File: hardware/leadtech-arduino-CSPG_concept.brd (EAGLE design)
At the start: 53.3 x 80 mm, 49 parts, among them IC1 OP-AMP, IC3 4050D, J1 CON_HEADER_1X08-PTH, J2 CON_HEADER_1X04, J3 CON_HEADER_1X03-PTH, J9 CON_HEADER_1X02-PTH, Q1 16Mhz, U1 DS1302, U3 PL2303HX

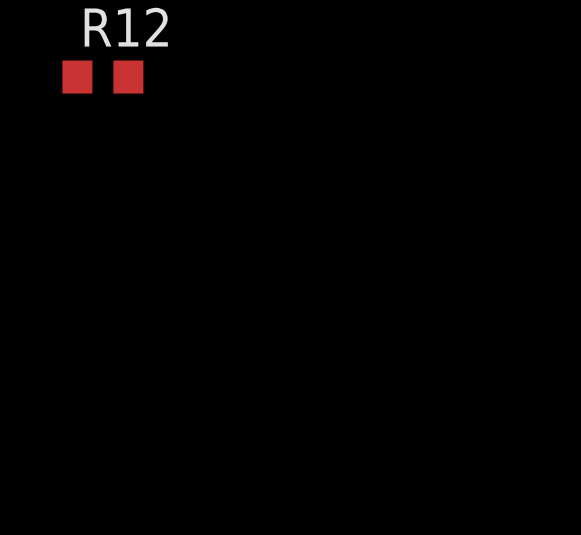
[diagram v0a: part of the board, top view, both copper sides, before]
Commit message: add power source manager op-amp wiring
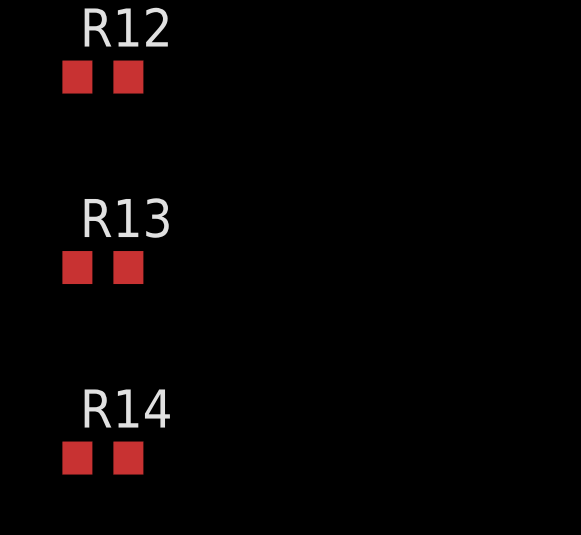
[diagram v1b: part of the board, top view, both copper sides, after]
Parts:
- added R13, R14: 10K, dp_devices.v6:R603
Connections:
- new net N$6: IC1.6, IC1.7
- new net N$9: IC1.5, R13.1, R14.2
- net +5V: now also R13.2
- net GND: now also R14.1
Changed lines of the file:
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@@
 <attribute name="VALUE" x="-24.892" y="-25.146" size="1.27" layer="27" font="vector" ratio="10"/>
+</element>
+<element name="R13" library="dp_devices.v6" package="R603" value="10K" x="-24.13" y="-29.21" smashed="yes">
+<attribute name="NAME" x="-24.892" y="-28.194" size="1.27" layer="25" font="vector" ratio="10"/>
+<attribute name="VALUE" x="-24.892" y="-31.496" size="1.27" layer="27" font="vector" ratio="10"/>
+</element>
+<element name="R14" library="dp_devices.v6" package="R603" value="10K" x="-24.13" y="-35.56" smashed="yes">
+<attribute name="NAME" x="-24.892" y="-34.544" size="1.27" layer="25" font="vector" ratio="10"/>
+<attribute name="VALUE" x="-24.892" y="-37.846" size="1.27" layer="27" font="vector" ratio="10"/>
 </element>
 </elements>
@@
 <contactref element="C1" pad="-"/>
 <contactref element="R12" pad="1"/>
+<contactref element="R14" pad="1"/>
 <wire x1="77.47" y1="76.2" x2="84.3534" y2="71.755" width="0" layer="19" extent="1-1"/>
 <wire x1="80.43" y1="59.69" x2="84.3534" y2="71.755" width="0" layer="19" extent="1-1"/>
@@
 <wire x1="-24.46" y1="-13.97" x2="-15" y2="-15.85" width="0" layer="19" extent="1-1"/>
 <wire x1="-24.98" y1="-22.86" x2="-24.46" y2="-13.97" width="0" layer="19" extent="1-1"/>
+<wire x1="-24.98" y1="-35.56" x2="-24.98" y2="-22.86" width="0" layer="19" extent="1-1"/>
 <wire x1="82.13" y1="22.86" x2="80.43" y2="59.69" width="0" layer="19" extent="1-1"/>
 <wire x1="86.995" y1="14.17" x2="82.13" y2="22.86" width="0" layer="19" extent="1-1"/>
@@
 <contactref element="VREG2" pad="3"/>
 <contactref element="Q2" pad="2"/>
+<contactref element="R13" pad="2"/>
 <wire x1="80.43" y1="22.86" x2="96.1" y2="41.91" width="0" layer="19" extent="1-1"/>
 <wire x1="83.185" y1="14.17" x2="80.43" y2="22.86" width="0" layer="19" extent="1-1"/>
@@
 <wire x1="-5.4" y1="-9.99" x2="1.905" y2="-7.36" width="0" layer="19" extent="1-1"/>
 <wire x1="-10.4" y1="-15.85" x2="-5.4" y2="-9.99" width="0" layer="19" extent="1-1"/>
+<wire x1="-23.28" y1="-29.21" x2="-10.4" y2="-15.85" width="0" layer="19" extent="1-1"/>
 </signal>
 <signal name="N$8">
@@
 <wire x1="-5.5" y1="-16.51" x2="5.08" y2="40.64" width="0" layer="19" extent="1-1"/>
 </signal>
+<signal name="N$6">
+<contactref element="IC1" pad="6"/>
+<contactref element="IC1" pad="7"/>
+<wire x1="3.175" y1="-7.36" x2="4.445" y2="-7.36" width="0" layer="19" extent="1-1"/>
+</signal>
+<signal name="N$9">
+<contactref element="IC1" pad="5"/>
+<contactref element="R13" pad="1"/>
+<contactref element="R14" pad="2"/>
+<wire x1="-24.98" y1="-29.21" x2="-23.28" y2="-35.56" width="0" layer="19" extent="1-1"/>
+<wire x1="5.715" y1="-7.36" x2="-24.98" y2="-29.21" width="0" layer="19" extent="1-1"/>
+</signal>
 </signals>

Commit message: continue routing board
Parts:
- removed VREG1: 7805, dp_devices.v6:TO-220V
- removed VREG2: 3.3V, dp_devices.v6:SOT-223
- added C16: 0.1uF, rcl:C0603
- added J4: CON_HEADER_1X02-PTH, dp_devices.v6:M1X2
- added U2: VREG-78M05, trosh_devices.eagle.v9:DPAK-3
- added U4: MP1584EN_MODULE, trosh_devices.eagle.v9:MP1584EN_DCDC_MODULE
- added U5: VREG-RT9163-3.3V, trosh_devices.eagle.v9:SOT-223
- moved C5 86.2 mm to (68.3, 6.35), turned to 270 degrees
- moved USB1 85.4 mm to (74.7, 14.0), turned to 90 degrees
- moved R12 80.7 mm to (44.5, 19.7), turned to 90 degrees
- moved L1 79.3 mm to (68.3, 10.8), turned to 90 degrees
- moved C1 78.4 mm to (39.4, 33.7), turned to 270 degrees
- moved C4 77.1 mm to (57.1, 5.08)
- moved R3 73.6 mm to (65.4, 12.1), turned to 180 degrees
- moved L2 71.8 mm to (68.3, 17.1), turned to 270 degrees
- moved R4 71.4 mm to (65.4, 14.0), turned to 180 degrees
- moved Q2 70.4 mm to (57.1, 21.6), turned to 180 degrees
- moved R14 70.4 mm to (7.62, 27.3), turned to 270 degrees
- moved R6 69.2 mm to (65.4, 15.9), turned to 180 degrees
- moved R5 68.7 mm to (26.7, 45.7), turned to 90 degrees
- moved R13 65.8 mm to (9.53, 27.3), turned to 270 degrees
- moved U3 65.2 mm to (57.1, 11.4), turned to 270 degrees
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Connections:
- new net N$7: J4.1, U4.3, U4.4
- net +3V3: now also U5.3; no longer VREG2.2
- net +5V: now also C16.2, U2.3, U5.1; no longer VREG1.2, VREG2.3
- net GND: now also C16.1, J4.2, U2.2, U4.1, U4.2, U4.7, U4.8, U5.2, U5.4; no longer VREG1.1, VREG2.1
- net N$19: now also U4.5, U4.6
- net VIN: now also U2.1; no longer VREG1.3
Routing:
- net +5V: track 0.00 -> 41.8 mm, vias 0 -> 2
- net VUSB: track 0.00 -> 33.6 mm, vias 0 -> 3
- net VO33: track 0.00 -> 30.6 mm
- net N$4: track 0.00 -> 13.6 mm, vias 0 -> 2
- net N$19: track 0.00 -> 12.5 mm
- net N$14: track 0.00 -> 11.9 mm
- net VIN: track 0.00 -> 9.40 mm
- net N$7: track 0.00 -> 9.08 mm
- net N$13: track 0.00 -> 8.23 mm
- net N$12: track 0.00 -> 7.23 mm
- net N$11: track 0.00 -> 5.78 mm
- net N$21: track 0.00 -> 3.26 mm
- net N$17: track 0.00 -> 2.65 mm
- net N$18: track 0.00 -> 2.37 mm
- added copper zone on layer 1, net GND
- added copper zone on layer 1, net N$15
- added copper zone on layer 1, net N$16
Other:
- board size 53.3 x 80 mm -> 80 x 53.3 mm

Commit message: routing
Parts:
- added J5: CON_HEADER_1X02-PTH, dp_devices.v6:M1X2
- moved C14 34.4 mm to (85.1, 40.6)
- moved C3 23.8 mm to (26.7, 50.8), turned to 270 degrees
- moved C2 23.5 mm to (21.6, 50.8), turned to 90 degrees
- moved J9 22.0 mm to (74.3, 43.8), turned to 180 degrees
- moved R1 19.3 mm to (31.8, 43.2), turned to 0 degrees
- moved J3 19.1 mm to (2.54, 51.4)
- moved C13 17.1 mm to (24.1, 22.2), turned to 180 degrees
- moved Q1 17.1 mm to (24.1, 46.4), turned to 0 degrees
- moved D1 16.6 mm to (53.3, 47.6)
- moved R5 15.9 mm to (34.3, 31.8), turned to 0 degrees
- moved C1 12.8 mm to (50.8, 39.4), turned to 0 degrees
- moved J4 11.2 mm to (74.3, 57.1)
- moved U2 10.7 mm to (65.4, 55.8)
- moved C8 10.3 mm to (57.8, 50.8)
- moved C9 9.72 mm to (57.7, 44.5), turned to 0 degrees
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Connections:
- net GND: now also J5.2
- net SW1: now also J5.1
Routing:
- net +5V: track 41.8 -> 83.5 mm, vias 2 -> 3
- net RTC_CLOCK: track 0.00 -> 38.2 mm, vias 0 -> 2
- net RTC_DATA: track 0.00 -> 37.7 mm, vias 0 -> 2
- net SW1: track 0.00 -> 37.2 mm
- net VIN: track 9.40 -> 44.2 mm, vias 0 -> 1
- net UART_TX: track 0.00 -> 30.1 mm, vias 0 -> 2
- net RTC_EN: track 0.00 -> 28.6 mm, vias 0 -> 2
- net UART_RX: track 0.00 -> 23.4 mm
- net N$19: track 12.5 -> 26.6 mm
- net N$7: track 9.08 -> 22.8 mm
- net RFID_DATA: track 0.00 -> 13.5 mm
- net RFID_CLOCK: track 0.00 -> 12.2 mm
- net RFID_MOSI: track 0.00 -> 10.8 mm
- net N$10: track 0.00 -> 10.0 mm
- net N$8: track 0.00 -> 9.90 mm
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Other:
- board size 80 x 53.3 mm -> 80 x 61 mm

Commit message: routing
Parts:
- removed C14: 100uF, dp_devices.v6:CASE_B
- removed J3: CON_HEADER_1X03-PTH, dp_devices.v6:M1X3
- added R15: 100R, rcl:R0603
- C1: value 10uF -> 100uF
- U5: value VREG-RT9163-3.3V -> RT9163-3.3V
- moved R14 50.1 mm to (57.1, 19.7), turned to 180 degrees
- moved R13 48.0 mm to (57.1, 21.6), turned to 0 degrees
- moved C13 24.7 mm to (31.8, 45.7), turned to 0 degrees
- moved C15 10.4 mm to (41.9, 40.0), turned to 90 degrees
- moved C11 8.52 mm to (19.7, 21.6)
- moved R12 4.30 mm to (43.8, 22.9), turned to 270 degrees
- moved C12 4.12 mm to (29.6, 21.6), turned to 270 degrees
- moved C16 3.81 mm to (54.6, 26.0), turned to 180 degrees
- moved IC3 2.89 mm to (38.7, 47.6), turned to 90 degrees
- moved Q2 1.91 mm to (63.5, 19.7)
- moved L1 0.26 mm to (68.6, 10.8)
- moved L2 0.26 mm to (68.6, 17.1)
- flipped D1 to the top
- flipped G1 to the top, turned to 270 degrees
- renumbered U$1 to U6
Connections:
- removed net N$1: J3.3
- removed net N$2: J3.2
- new net N$20: R15.2, SG1.+
- net +3V3: no longer C14.+
- net GND: no longer C14.-, J3.1
- net PIEZO: now also R15.1; no longer SG1.+
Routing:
- net +5V: track 83.5 -> 225.0 mm, vias 3 -> 10
- net +3V3: track 4.92 -> 54.4 mm, vias 0 -> 2
- net DISPLAY_I2C_DATA: track 0.00 -> 37.8 mm, vias 0 -> 1
- net DISPLAY_I2C_CLOCK: track 0.00 -> 35.7 mm, vias 0 -> 1
- net PIEZO: track 0.00 -> 31.8 mm
- net RFID_DATA_3V: track 0.00 -> 23.2 mm, vias 0 -> 1
- net RFID_CLOCK_3V: track 0.00 -> 20.0 mm, vias 0 -> 1
- net RFID_MISO: track 9.48 -> 28.1 mm
- net RFID_MOSI_3V: track 0.00 -> 16.8 mm, vias 0 -> 1
- net RFID_RESET_3V: track 0.00 -> 15.8 mm, vias 0 -> 1
- net RFID_MOSI: track 10.8 -> 23.8 mm
- net RFID_RESET: track 6.06 -> 17.6 mm
- net N$24: track 0.00 -> 10.6 mm
- net RFID_CLOCK: track 12.2 -> 22.4 mm
- net RFID_DATA: track 13.5 -> 20.9 mm
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- added copper zone on layer 16, net GND
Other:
- board text added: "3V3"
- board text added: "5V"
- board text added: "BUTTON"
- board text added: "CLK"
- board text added: "DATA"
- board text added: "DISPLAY"
- board text added: "GND"
- board text added: "LEADTECH INC."
- board text added: "MAR 2020"
- board text added: "MISO"
- board text added: "MOSI"
- board text added: "NC"
- board text added: "PREPAID METERING MAIN BOARD V1.0"
- board text added: "PWR"
- board text added: "RF ID READER"
- board text added: "RST"
- board text added: "SDA"
- board text added: "v.trocio 2020"

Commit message: 1
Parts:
- removed G1: CR2032H, battery:CR2032H
- added BATT1: CR2032, trosh_devices.eagle.v9:CR2032-BS-6
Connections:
- net GND: now also BATT1.2; no longer G1.-
- net N$24: now also BATT1.1; no longer G1.+
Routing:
- net N$24: track 10.6 -> 5.30 mm
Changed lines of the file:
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@@
 <?xml version="1.0" encoding="utf-8"?>
 <!DOCTYPE eagle SYSTEM "eagle.dtd">
-<eagle version="9.4.2">
+<eagle version="9.1.3">
 <drawing>
 <settings>
@@
 <text x="4.45" y="36.195" size="1.651" layer="26" font="vector" ratio="12" rot="SMR0" align="center-right">BUTTON</text>
 <text x="4.45" y="33.655" size="1.651" layer="26" font="vector" ratio="12" rot="SMR0" align="center-right">GND</text>
+<circle x="28.575" y="10.16" radius="10" width="0.1524" layer="51"/>
 </plain>
 <attributes>
@@
 <attribute name="VALUE" x="50.546" y="49.617" size="1.27" layer="27" ratio="10" rot="R270"/>
 </element>
-<element name="G1" library="battery" library_urn="urn:adsk.eagle:library:109" package="CR2032H" package3d_urn="urn:adsk.eagle:package:4585/1" value="CR2032H" x="27.305" y="10.12" smashed="yes" rot="R270">
-<attribute name="NAME" x="36.195" y="17.7" size="1.27" layer="25" font="vector" ratio="12" rot="R180" align="center"/>
-<attribute name="VALUE" x="25.4" y="5.04" size="1.27" layer="27" ratio="10"/>
-</element>
 <element name="J9" library="dp_devices.v6" package="M1X2" value="CON_HEADER_1X02-PTH" x="74.255" y="43.815" smashed="yes" rot="R180">
 <attribute name="NAME" x="78.105" y="43.815" size="1.27" layer="25" font="vector" ratio="12" rot="R180" align="center"/>
@@
 <attribute name="VALUE" x="9.525" y="16.51" size="1.27" layer="27" rot="R180"/>
 </element>
+<element name="BATT1" library="trosh_devices.eagle.v9" package="CR2032-BS-6" value="CR2032" x="28.575" y="10.16"/>
 </elements>
 <signals>
@@
 <contactref element="C4" pad="2"/>
 <contactref element="U1" pad="P4"/>
-<contactref element="G1" pad="-"/>
 <contactref element="C10" pad="2"/>
 <contactref element="U6" pad="63"/>
@@
 </polygon>
 <via x="59.055" y="19.685" extent="1-16" drill="0.35"/>
+<contactref element="BATT1" pad="2"/>
+<wire x1="65.405" y1="55.88" x2="75.565" y2="57.11" width="0" layer="19" extent="1-1"/>
+<wire x1="57.365" y1="55.84" x2="65.405" y2="55.88" width="0" layer="19" extent="1-1"/>
+<wire x1="56.185" y1="50.8" x2="57.365" y2="55.84" width="0" layer="19" extent="1-1"/>
+<wire x1="55.88" y1="48.895" x2="56.185" y2="50.8" width="0" layer="19" extent="1-1"/>
+<wire x1="54.229" y1="50.8" x2="56.185" y2="50.8" width="0" layer="19" extent="1-1"/>
+<wire x1="55.88" y1="46.355" x2="55.88" y2="48.895" width="0" layer="19" extent="1-1"/>
+<wire x1="56.185" y1="44.45" x2="55.88" y2="46.355" width="0" layer="19" extent="1-1"/>
+<wire x1="55.88" y1="42.545" x2="56.185" y2="44.45" width="0" layer="19" extent="1-1"/>
+<wire x1="49.2" y1="39.37" x2="55.88" y2="42.545" width="0" layer="19" extent="1-1"/>
+<wire x1="46.99" y1="39.37" x2="49.2" y2="39.37" width="0" layer="19" extent="1-1"/>
+<wire x1="46.99" y1="37.465" x2="46.99" y2="39.37" width="0" layer="19" extent="1-1"/>
+<wire x1="47.65" y1="33.02" x2="46.99" y2="37.465" width="0" layer="19" extent="1-1"/>
+<wire x1="41.91" y1="39.195" x2="46.99" y2="39.37" width="0" layer="19" extent="1-1"/>
+<wire x1="41.91" y1="38.1" x2="41.91" y2="39.195" width="0" layer="19" extent="1-1"/>
+<wire x1="53.95" y1="33.02" x2="47.65" y2="33.02" width="0" layer="19" extent="1-1"/>
+<wire x1="55.88" y1="33.02" x2="53.95" y2="33.02" width="0" layer="19" extent="1-1"/>
+<wire x1="58.634" y1="28.003" x2="55.88" y2="33.02" width="0" layer="19" extent="1-1"/>
+<wire x1="58.634" y1="25.463" x2="58.634" y2="28.003" width="0" layer="19" extent="1-1"/>
+<wire x1="55.46" y1="26.035" x2="58.634" y2="25.463" width="0" layer="19" extent="1-1"/>
+<wire x1="59.055" y1="19.685" x2="58.634" y2="25.463" width="0" layer="19" extent="1-1"/>
+<wire x1="58" y1="19.685" x2="59.055" y2="19.685" width="0" layer="19" extent="1-1"/>
+<wire x1="56.3" y1="17.74" x2="58" y2="19.685" width="0" layer="19" extent="1-1"/>
+<wire x1="54.991" y1="17.78" x2="56.3" y2="17.74" width="0" layer="19" extent="1-1"/>
+<wire x1="59.055" y1="13.97" x2="56.3" y2="17.74" width="0" layer="19" extent="1-1"/>
+<wire x1="60.425" y1="13.665" x2="59.055" y2="13.97" width="0" layer="19" extent="1-1"/>
+<wire x1="60.425" y1="14.315" x2="60.425" y2="13.665" width="0" layer="19" extent="1-1"/>
+<wire x1="62.23" y1="13.97" x2="60.425" y2="13.665" width="0" layer="19" extent="1-1"/>
+<wire x1="55.372" y1="11.771" x2="59.055" y2="13.97" width="0" layer="19" extent="1-1"/>
+<wire x1="53.875" y1="11.715" x2="55.372" y2="11.771" width="0" layer="19" extent="1-1"/>
+<wire x1="52.578" y1="11.517" x2="53.875" y2="11.715" width="0" layer="19" extent="1-1"/>
+<wire x1="57.912" y1="8.977" x2="55.372" y2="11.771" width="0" layer="19" extent="1-1"/>
+<wire x1="60.425" y1="9.115" x2="57.912" y2="8.977" width="0" layer="19" extent="1-1"/>
+<wire x1="62.357" y1="9.358" x2="60.425" y2="9.115" width="0" layer="19" extent="1-1"/>
+<wire x1="49.95" y1="14.565" x2="52.578" y2="11.517" width="0" layer="19" extent="1-1"/>
+<wire x1="56.3" y1="5.04" x2="57.912" y2="8.977" width="0" layer="19" extent="1-1"/>
+<wire x1="49.53" y1="19.685" x2="49.95" y2="14.565" width="0" layer="19" extent="1-1"/>
+<wire x1="48" y1="19.685" x2="49.53" y2="19.685" width="0" layer="19" extent="1-1"/>
+<wire x1="47.625" y1="8.89" x2="52.578" y2="11.517" width="0" layer="19" extent="1-1"/>
+<wire x1="47.625" y1="7.185" x2="47.625" y2="8.89" width="0" layer="19" extent="1-1"/>
+<wire x1="43.815" y1="23.71" x2="48" y2="19.685" width="0" layer="19" extent="1-1"/>
+<wire x1="48.768" y1="26.035" x2="43.815" y2="23.71" width="0" layer="19" extent="1-1"/>
+<wire x1="42.545" y1="2.325" x2="47.625" y2="7.185" width="0" layer="19" extent="1-1"/>
+<wire x1="41.275" y1="2.54" x2="42.545" y2="2.325" width="0" layer="19" extent="1-1"/>
+<wire x1="68.326" y1="5.36" x2="62.357" y2="9.358" width="0" layer="19" extent="1-1"/>
+<wire x1="68.58" y1="17.995" x2="62.23" y2="13.97" width="0" layer="19" extent="1-1"/>
+<wire x1="43.815" y1="52.07" x2="54.229" y2="50.8" width="0" layer="19" extent="1-1"/>
+<wire x1="41.8084" y1="52.03" x2="43.815" y2="52.07" width="0" layer="19" extent="1-1"/>
+<wire x1="43.81" y1="58.5" x2="43.815" y2="52.07" width="0" layer="19" extent="1-1"/>
+<wire x1="32.6" y1="45.72" x2="41.8084" y2="52.03" width="0" layer="19" extent="1-1"/>
+<wire x1="26.67" y1="51.75" x2="32.6" y2="45.72" width="0" layer="19" extent="1-1"/>
+<wire x1="21.59" y1="51.75" x2="26.67" y2="51.75" width="0" layer="19" extent="1-1"/>
+<wire x1="25.495" y1="40.77" x2="32.6" y2="45.72" width="0" layer="19" extent="1-1"/>
+<wire x1="77.176" y1="25.463" x2="68.58" y2="17.995" width="0" layer="19" extent="1-1"/>
+<wire x1="77.176" y1="28.003" x2="77.176" y2="25.463" width="0" layer="19" extent="1-1"/>
+<wire x1="75.525" y1="43.815" x2="75.565" y2="57.11" width="0" layer="19" extent="1-1"/>
+<wire x1="29.591" y1="20.74" x2="43.815" y2="23.71" width="0" layer="19" extent="1-1"/>
+<wire x1="28.695" y1="25.27" x2="29.591" y2="20.74" width="0" layer="19" extent="1-1"/>
+<wire x1="20.695" y1="25.27" x2="28.695" y2="25.27" width="0" layer="19" extent="1-1"/>
+<wire x1="19.685" y1="20.74" x2="20.695" y2="25.27" width="0" layer="19" extent="1-1"/>
+<wire x1="14.075" y1="10.16" x2="19.685" y2="20.74" width="0" layer="19" extent="1-1"/>
+<wire x1="7.62" y1="3.175" x2="14.075" y2="10.16" width="0" layer="19" extent="1-1"/>
+<wire x1="2.54" y1="24.13" x2="19.685" y2="20.74" width="0" layer="19" extent="1-1"/>
+<wire x1="2.54" y1="33.655" x2="2.54" y2="24.13" width="0" layer="19" extent="1-1"/>
 </signal>
 <signal name="+5V">
@@
 <signal name="N$24">
 <contactref element="U1" pad="P8"/>
-<contactref element="G1" pad="+"/>
 <wire x1="41.435" y1="11.865" x2="43.815" y2="11.865" width="0.4064" layer="1"/>
-<wire x1="38.1" y1="5.04" x2="38.1" y2="8.53" width="0.4064" layer="1"/>
-<wire x1="38.1" y1="8.53" x2="41.435" y2="11.865" width="0.4064" layer="1"/>
+<wire x1="39.37" y1="9.8" x2="41.435" y2="11.865" width="0.4064" layer="1"/>
+<contactref element="BATT1" pad="1"/>
+<wire x1="43.815" y1="11.865" x2="43.075" y2="10.16" width="0" layer="19" extent="1-1"/>
 </signal>
 <signal name="RTC_EN">

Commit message: routing
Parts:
- removed J2: CON_HEADER_1X04, dp_devices.v6:M1X4
- removed J4: CON_HEADER_1X02-PTH, dp_devices.v6:M1X2
- removed U$2: (no value), trosh_devices.eagle.v9:GIZDUINOX
- added C14: 0.1uF, rcl:C0603
- added C17, C18: 10uF, dp_devices.v6:CASE_B
- added J3: CON_HX42003_2, trosh_devices.eagle.v9:HX42003-2WAF
- added J6: 2510-4AGW, trosh_devices.eagle.v9:KF2510-4AGW-2
- added MOD1: ESP8266-07, trosh_devices.eagle.v9:ESP8266-07
- added R16, R17, R18, R19, R20: 10K, dp_devices.v6:R603
- added U7: AZ1117CH2-3.3TRG1, trosh_devices.eagle.v9:SOT-223
- BATT1: value CR2032 -> CR2032-BS-6-1
- moved J5 32.4 mm to (24.8, 58.5), turned to 180 degrees
- moved XTAL1 7.11 mm to (54.7, 3.05)
- moved C4 5.72 mm to (62.9, 5.08), turned to 0 degrees
- moved R10 4.49 mm to (6.99, 14.6)
- moved R2 4.49 mm to (6.99, 17.1)
- moved U1 3.59 mm to (48.3, 6.99)
- moved R15 2.29 mm to (10.8, 13.3), turned to 270 degrees
- moved SG1 1.42 mm to (6.35, 6.35)
- moved C5 0.26 mm to (68.6, 6.35)
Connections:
- new net +3V3_ESP: C14.2, C17.+, MOD1.8, U7.3
- new net ESP_RXD: IC3.14, U6.28
- new net ESP_TXD: MOD1.16, U6.27
- new net N$1: MOD1.1, R16.1
- new net N$2: MOD1.3, R17.1
- new net N$25: MOD1.10, R18.2
- new net N$26: MOD1.11, R19.2
- new net N$27: MOD1.12, R20.2
- new net N$28: IC3.15, MOD1.15
- net +3V3: now also R16.2, R17.2, R19.1, R20.1
- net +5V: now also C18.+, J6.4, U7.1; no longer J2.1
- net DISPLAY_I2C_CLOCK: now also J6.2; no longer J2.3
- net DISPLAY_I2C_DATA: now also J6.1; no longer J2.4
- net GND: now also C14.1, C17.-, C18.-, J3.2, J6.3, MOD1.9, R18.1, U7.2, U7.4; no longer J2.2, J4.2
- net N$22: now also XTAL1.P1; no longer XTAL1.P2
- net N$23: now also XTAL1.P2; no longer XTAL1.P1
- net N$7: now also J3.1; no longer J4.1
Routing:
- net SW1: track 37.0 -> 2.50 mm
- net N$7: track 22.8 -> 15.6 mm
- net DISPLAY_I2C_DATA: track 37.8 -> 33.2 mm
- net DISPLAY_I2C_CLOCK: track 35.7 -> 31.4 mm
- net N$23: track 2.78 -> 6.99 mm
- net +5V: track 225.0 -> 221.0 mm
- net RTC_DATA: track 36.5 -> 40.1 mm
- net RTC_EN: track 26.7 -> 30.3 mm
- net RTC_CLOCK: track 37.3 -> 40.9 mm
- net VO33: track 30.4 -> 32.7 mm
- net N$20: track 3.98 -> 6.03 mm
- net PIEZO: track 31.8 -> 30.5 mm
- net N$24: track 5.30 -> 4.11 mm
- net N$22: track 5.85 -> 4.87 mm
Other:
- board text added: "v.trocio"
- board text removed: "v.trocio 2020"
